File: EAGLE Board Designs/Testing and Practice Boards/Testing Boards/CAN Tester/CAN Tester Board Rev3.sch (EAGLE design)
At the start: 10 parts, among them J1 CONNECTOR-CAN_μF_S_RA_, J2 CONNECTOR-2_MICROFIT_SMD_RIGH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, U1 MCP2562FD

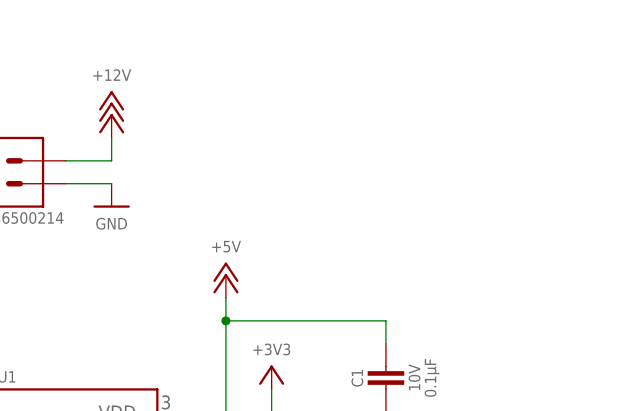
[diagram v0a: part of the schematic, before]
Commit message: added lin reg
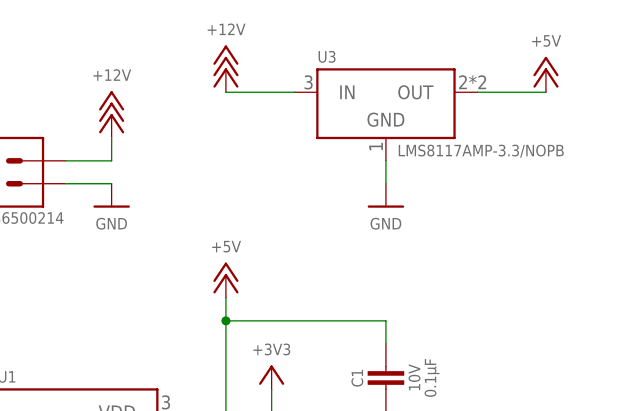
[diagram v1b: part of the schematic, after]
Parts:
- added U3: VOLTAGE_REGULATOR_SOT-223_3.3V, HyTechDevices:VOLTAGE_REGULATOR_SOT-223_3.3V
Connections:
- net +12V: now also U3.IN
- net +5V: now also U3.OUT
- net GND: now also U3.GND
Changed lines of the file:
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@@
 <part name="P9" library="HyTechSupplies" deviceset="+12V" device=""/>
 <part name="P10" library="HyTechSupplies" deviceset="+5V" device=""/>
+<part name="U3" library="HyTechDevices" deviceset="VOLTAGE_REGULATOR_?_*" device="SOT-223" technology="3.3V"/>
+<part name="P11" library="HyTechSupplies" deviceset="+12V" device=""/>
+<part name="P12" library="HyTechSupplies" deviceset="GND" device=""/>
+<part name="P13" library="HyTechSupplies" deviceset="+5V" device=""/>
 </parts>
 <sheets>
@@
 <attribute name="VALUE" x="58.42" y="109.22" size="1.27" layer="96" align="bottom-center"/>
 </instance>
+<instance part="U3" gate="G$1" x="106.68" y="109.22" smashed="yes">
+<attribute name="NAME" x="106.68" y="109.982" size="1.27" layer="95"/>
+<attribute name="MPN" x="115.57" y="100.838" size="1.27" layer="96" align="top-left"/>
+</instance>
+<instance part="P11" gate="1" x="96.52" y="109.22" smashed="yes">
+<attribute name="VALUE" x="96.52" y="113.03" size="1.27" layer="96" align="bottom-center"/>
+</instance>
+<instance part="P12" gate="1" x="114.3" y="93.98" smashed="yes">
+<attribute name="VALUE" x="114.3" y="92.71" size="1.27" layer="96" align="top-center"/>
+</instance>
+<instance part="P13" gate="1" x="132.08" y="109.22" smashed="yes">
+<attribute name="VALUE" x="132.08" y="111.76" size="1.27" layer="96" align="bottom-center"/>
+</instance>
 </instances>
 <busses>
@@
 <pinref part="P8" gate="1" pin="GND"/>
 <wire x1="78.74" y1="96.52" x2="83.82" y2="96.52" width="0.1524" layer="91"/>
+</segment>
+<segment>
+<pinref part="U3" gate="G$1" pin="GND"/>
+<pinref part="P12" gate="1" pin="GND"/>
+<wire x1="114.3" y1="99.06" x2="114.3" y2="96.52" width="0.1524" layer="91"/>
 </segment>
 </net>
@@
 <wire x1="54.61" y1="104.14" x2="54.61" y2="100.33" width="0.1524" layer="91"/>
 </segment>
+<segment>
+<pinref part="U3" gate="G$1" pin="OUT"/>
+<pinref part="P13" gate="1" pin="+5V"/>
+<wire x1="124.46" y1="106.68" x2="132.08" y2="106.68" width="0.1524" layer="91"/>
+</segment>
 </net>
 <net name="+3V3" class="0">
@@
 <wire x1="83.82" y1="99.06" x2="83.82" y2="101.6" width="0.1524" layer="91"/>
 </segment>
-</net>
+<segment>
+<pinref part="P11" gate="1" pin="+12V"/>
+<pinref part="U3" gate="G$1" pin="IN"/>
+<wire x1="96.52" y1="106.68" x2="104.14" y2="106.68" width="0.1524" layer="91"/>
+</segment>
+</net>

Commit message: made changes to board
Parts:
- removed U3: VOLTAGE_REGULATOR_SOT-223_3.3V, HyTechDevices:VOLTAGE_REGULATOR_SOT-223_3.3V
- added U2: VOLTAGE_REGULATOR_SOT-89_12V, HyTechDevices:VOLTAGE_REGULATOR_SOT-89_12V
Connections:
- net +12V: now also U2.IN; no longer U3.IN
- net +3V3: now also A1.3.3V
- net +5V: now also U2.OUT; no longer U3.OUT
- net GND: now also A1.GND, U2.GND; no longer U3.GND
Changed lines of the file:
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@@
 <setting verticaltext="up"/>
 </settings>
-<grid distance="0.1" unitdist="inch" unit="inch" style="lines" multiple="1" display="no" altdistance="0.01" altunitdist="inch" altunit="inch"/>
+<grid distance="0.1" unitdist="inch" unit="inch" style="lines" multiple="1" display="yes" altdistance="0.01" altunitdist="inch" altunit="inch"/>
 <layers>
 <layer number="1" name="Top" color="4" fill="1" visible="no" active="no"/>
@@
 <part name="P9" library="HyTechSupplies" deviceset="+12V" device=""/>
 <part name="P10" library="HyTechSupplies" deviceset="+5V" device=""/>
-<part name="U3" library="HyTechDevices" deviceset="VOLTAGE_REGULATOR_?_*" device="SOT-223" technology="3.3V"/>
 <part name="P11" library="HyTechSupplies" deviceset="+12V" device=""/>
 <part name="P12" library="HyTechSupplies" deviceset="GND" device=""/>
 <part name="P13" library="HyTechSupplies" deviceset="+5V" device=""/>
+<part name="U2" library="HyTechDevices" deviceset="VOLTAGE_REGULATOR_?_*" device="SOT-89" technology="12V"/>
+<part name="P14" library="HyTechSupplies" deviceset="+3V3" device=""/>
+<part name="P15" library="HyTechSupplies" deviceset="GND" device=""/>
 </parts>
 <sheets>
@@
 <plain>
 <text x="76.2" y="40.64" size="2.54" layer="95">CAN Termination</text>
+<frame x1="0" y1="0" x2="177.8" y2="152.4" columns="8" rows="5" layer="91"/>
 </plain>
 <instances>
-<instance part="A1" gate="G$1" x="31.75" y="105.41" smashed="yes"/>
+<instance part="A1" gate="G$1" x="30.48" y="106.68" smashed="yes"/>
 <instance part="U1" gate="G$1" x="71.12" y="73.66" smashed="yes">
 <attribute name="NAME" x="71.12" y="74.422" size="1.27" layer="95"/>
@@
 <attribute name="VALUE" x="58.42" y="109.22" size="1.27" layer="96" align="bottom-center"/>
 </instance>
-<instance part="U3" gate="G$1" x="106.68" y="109.22" smashed="yes">
+<instance part="P11" gate="1" x="96.52" y="109.22" smashed="yes">
+<attribute name="VALUE" x="96.52" y="113.03" size="1.27" layer="96" align="bottom-center"/>
+</instance>
+<instance part="P12" gate="1" x="114.3" y="93.98" smashed="yes">
+<attribute name="VALUE" x="114.3" y="92.71" size="1.27" layer="96" align="top-center"/>
+</instance>
+<instance part="P13" gate="1" x="132.08" y="109.22" smashed="yes">
+<attribute name="VALUE" x="132.08" y="111.76" size="1.27" layer="96" align="bottom-center"/>
+</instance>
+<instance part="U2" gate="G$1" x="106.68" y="109.22" smashed="yes">
 <attribute name="NAME" x="106.68" y="109.982" size="1.27" layer="95"/>
 <attribute name="MPN" x="115.57" y="100.838" size="1.27" layer="96" align="top-left"/>
 </instance>
-<instance part="P11" gate="1" x="96.52" y="109.22" smashed="yes">
-<attribute name="VALUE" x="96.52" y="113.03" size="1.27" layer="96" align="bottom-center"/>
-</instance>
-<instance part="P12" gate="1" x="114.3" y="93.98" smashed="yes">
-<attribute name="VALUE" x="114.3" y="92.71" size="1.27" layer="96" align="top-center"/>
-</instance>
-<instance part="P13" gate="1" x="132.08" y="109.22" smashed="yes">
-<attribute name="VALUE" x="132.08" y="111.76" size="1.27" layer="96" align="bottom-center"/>
+<instance part="P14" gate="G$1" x="60.96" y="101.6" smashed="yes">
+<attribute name="VALUE" x="60.96" y="102.87" size="1.27" layer="96" align="bottom-center"/>
+</instance>
+<instance part="P15" gate="1" x="25.4" y="58.42" smashed="yes">
+<attribute name="VALUE" x="25.4" y="57.15" size="1.27" layer="96" align="top-center"/>
 </instance>
 </instances>
@@
 <pinref part="A1" gate="G$1" pin="(CTX1)D1"/>
 <pinref part="U1" gate="G$1" pin="TXD"/>
-<wire x1="54.61" y1="64.77" x2="68.58" y2="64.77" width="0.1524" layer="91"/>
-<wire x1="68.58" y1="64.77" x2="68.58" y2="66.04" width="0.1524" layer="91"/>
-<label x="58.42" y="68.58" size="1.27" layer="95" xref="yes"/>
+<wire x1="53.34" y1="66.04" x2="68.58" y2="66.04" width="0.1524" layer="91"/>
+<label x="55.88" y="66.04" size="1.27" layer="95" align="top-left"/>
 </segment>
 </net>
@@
 <pinref part="A1" gate="G$1" pin="(CRX1)D0"/>
 <pinref part="U1" gate="G$1" pin="RXD"/>
-<wire x1="54.61" y1="62.23" x2="68.58" y2="62.23" width="0.1524" layer="91"/>
-<wire x1="68.58" y1="62.23" x2="68.58" y2="63.5" width="0.1524" layer="91"/>
-<label x="55.88" y="58.42" size="1.27" layer="95" xref="yes"/>
+<wire x1="53.34" y1="63.5" x2="68.58" y2="63.5" width="0.1524" layer="91"/>
+<label x="55.88" y="63.5" size="1.27" layer="95" align="top-left"/>
 </segment>
 </net>
@@
 <wire x1="114.3" y1="58.42" x2="114.3" y2="60.96" width="0.1524" layer="91"/>
 <wire x1="114.3" y1="60.96" x2="106.68" y2="60.96" width="0.1524" layer="91"/>
-<junction x="114.3" y="58.42"/>
 </segment>
 <segment>
@@
 <pinref part="J1" gate="G$1" pin="GND"/>
 <pinref part="P7" gate="1" pin="GND"/>
-<wire x1="48.26" y1="38.1" x2="48.26" y2="35.56" width="0.1524" layer="91"/>
-<wire x1="48.26" y1="35.56" x2="50.8" y2="35.56" width="0.1524" layer="91"/>
+<wire x1="48.26" y1="38.1" x2="50.8" y2="38.1" width="0.1524" layer="91"/>
+<wire x1="50.8" y1="38.1" x2="50.8" y2="35.56" width="0.1524" layer="91"/>
 </segment>
 <segment>
@@
 </segment>
 <segment>
-<pinref part="U3" gate="G$1" pin="GND"/>
 <pinref part="P12" gate="1" pin="GND"/>
 <wire x1="114.3" y1="99.06" x2="114.3" y2="96.52" width="0.1524" layer="91"/>
+<pinref part="U2" gate="G$1" pin="GND"/>
+</segment>
+<segment>
+<pinref part="A1" gate="G$1" pin="GND"/>
+<wire x1="27.94" y1="63.5" x2="25.4" y2="63.5" width="0.1524" layer="91"/>
+<pinref part="P15" gate="1" pin="GND"/>
+<wire x1="25.4" y1="63.5" x2="25.4" y2="60.96" width="0.1524" layer="91"/>
 </segment>
 </net>
@@
 </segment>
 <segment>
-<pinref part="P10" gate="1" pin="+5V"/>
-<pinref part="A1" gate="G$1" pin="VIN"/>
-<wire x1="58.42" y1="104.14" x2="54.61" y2="104.14" width="0.1524" layer="91"/>
-<wire x1="54.61" y1="104.14" x2="54.61" y2="100.33" width="0.1524" layer="91"/>
-</segment>
-<segment>
-<pinref part="U3" gate="G$1" pin="OUT"/>
 <pinref part="P13" gate="1" pin="+5V"/>
 <wire x1="124.46" y1="106.68" x2="132.08" y2="106.68" width="0.1524" layer="91"/>
+<pinref part="U2" gate="G$1" pin="OUT"/>
+<label x="124.46" y="104.14" size="1.778" layer="95"/>
+</segment>
+<segment>
+<pinref part="A1" gate="G$1" pin="VIN"/>
+<wire x1="53.34" y1="101.6" x2="58.42" y2="101.6" width="0.1524" layer="91"/>
+<pinref part="P10" gate="1" pin="+5V"/>
+<wire x1="58.42" y1="101.6" x2="58.42" y2="104.14" width="0.1524" layer="91"/>
 </segment>
 </net>
@@
 <junction x="101.6" y="68.58"/>
 </segment>
+<segment>
+<pinref part="A1" gate="G$1" pin="3.3V"/>
+<wire x1="53.34" y1="99.06" x2="60.96" y2="99.06" width="0.1524" layer="91"/>
+<pinref part="P14" gate="G$1" pin="+3V3"/>
+</segment>
 </net>
 <net name="CANH" class="1">
@@
 <pinref part="J1" gate="G$1" pin="+12V"/>
 <pinref part="P6" gate="1" pin="+12V"/>
-<wire x1="48.26" y1="45.72" x2="48.26" y2="48.26" width="0.1524" layer="91"/>
-<wire x1="48.26" y1="48.26" x2="50.8" y2="48.26" width="0.1524" layer="91"/>
+<wire x1="48.26" y1="45.72" x2="50.8" y2="45.72" width="0.1524" layer="91"/>
+<wire x1="50.8" y1="45.72" x2="50.8" y2="48.26" width="0.1524" layer="91"/>
 </segment>
 <segment>
@@
 <segment>
 <pinref part="P11" gate="1" pin="+12V"/>
-<pinref part="U3" gate="G$1" pin="IN"/>
 <wire x1="96.52" y1="106.68" x2="104.14" y2="106.68" width="0.1524" layer="91"/>
+<pinref part="U2" gate="G$1" pin="IN"/>
 </segment>
 </net>
@@
 which will not be processed correctly with this version.
 </note>
+<note version="9.0" severity="warning">
+Since Version 9.0, EAGLE supports the align property for labels.
+Labels in schematic will not be understood with this version. Update EAGLE to the latest version
+for full support of labels.
+</note>
 </compatibility>
